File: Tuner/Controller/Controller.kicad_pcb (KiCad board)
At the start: 2 copper layers, 96.8 x 99.3 mm, 175 parts, among them J1 Conn_02x05_Odd_Even, J10 Conn_01x05, J11 Conn_01x01, J12 Conn_01x02, J14 Conn_01x01, J15 Conn_01x02, J16 Conn_01x06, J17 Conn_01x01, J18 Conn_01x01, J19 Conn_01x01, J2 Conn_02x05_Odd_Even, J20 Conn_01x01, J21 Conn_01x01, J23 Conn_01x01, J26 Conn_01x02, J27 Conn_01x02, J28 Conn_01x02, J3 Conn_02x05_Odd_Even, J30 Conn_01x02, J4 Conn_02x05_Odd_Even, J5 Conn_02x05_Odd_Even, J6 Conn_01x02, J7 Conn_01x02, J8 Conn_01x06, Q1 2N3904, Q2 2N3904, Q3 2N3904, Q4 2N3904, Q5 2N3904, Q6 2N3904, Q7 2N3904, Q8 2N3904, U1 74LS393, U2 74HC14, U3 74HC86, U4 LM350_TO220

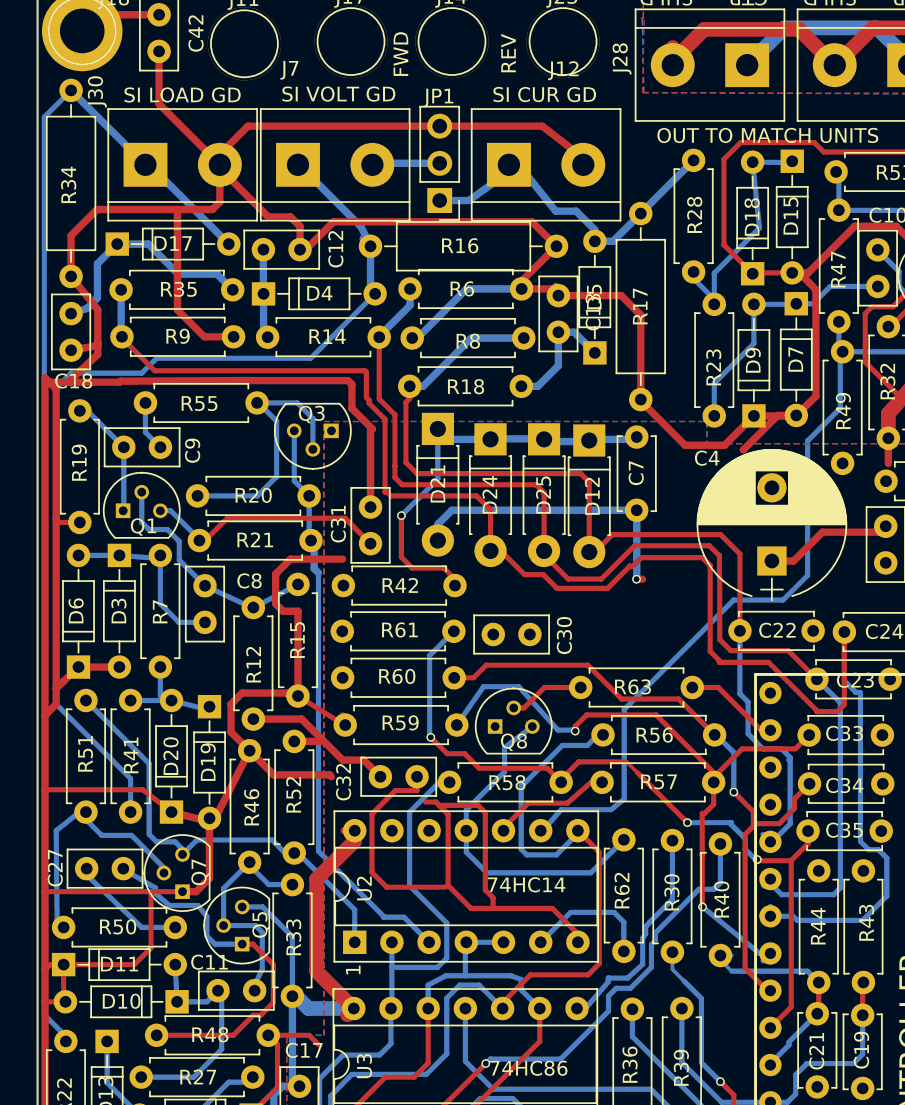
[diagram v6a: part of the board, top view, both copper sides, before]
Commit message: Fixed TandemMatch grounding problem
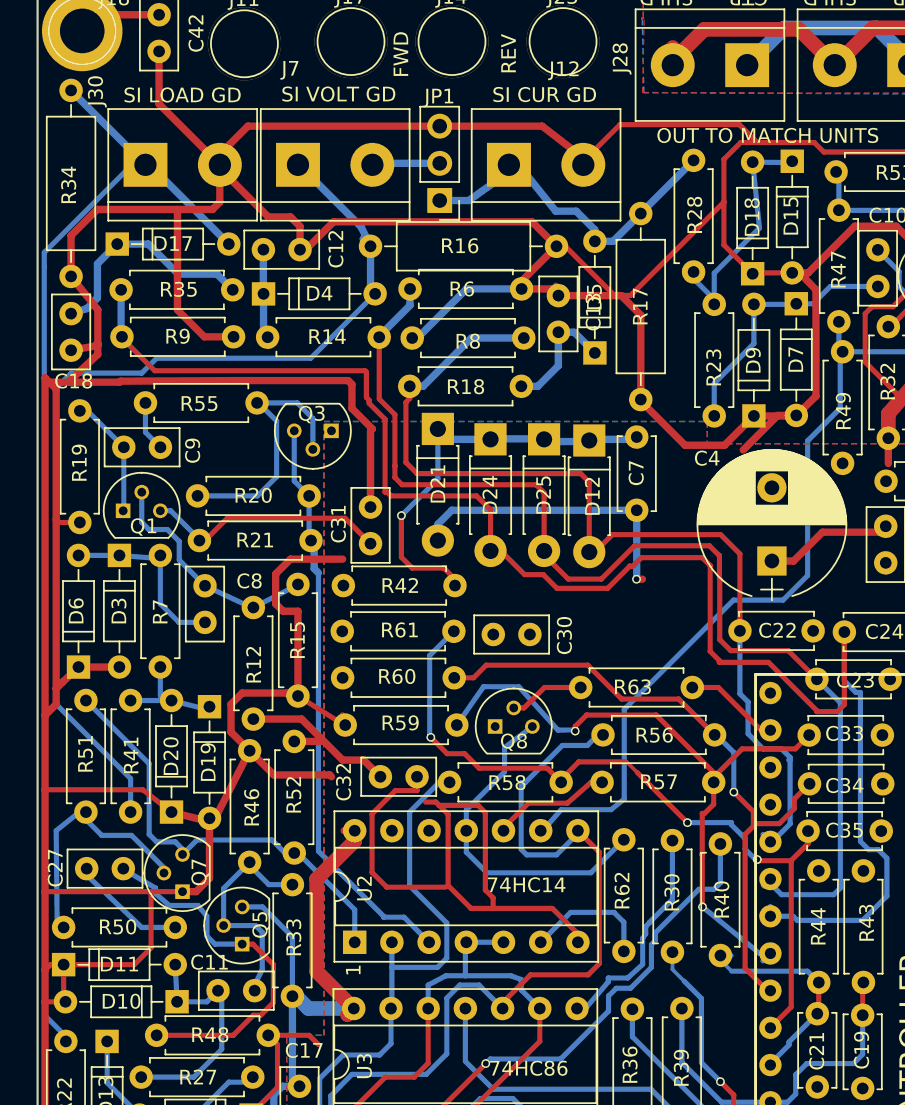
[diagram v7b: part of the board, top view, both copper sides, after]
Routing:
- net GND: track 622.5 -> 652.1 mm
- net XCur: track 82.0 -> 79.5 mm
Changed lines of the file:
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@@
     (thickness 1.6)
     (drawings 57)
-    (tracks 1583)
+    (tracks 1597)
     (zones 0)
     (modules 175)
@@
   )
   (setup
-    (last_trace_width 0.5)
+    (last_trace_width 0.35)
     (user_trace_width 0.35)
     (user_trace_width 0.5)
@@
   (segment (start 76.5302 99.187) (end 76.962 98.7552) (width 0.5) (layer F.Cu) (net 5) (status 30))
   (segment (start 77.0255 86.614) (end 76.30414 86.614) (width 0.5) (layer F.Cu) (net 5) (status 30))
+  (segment (start 94.7547 50.0634) (end 95.8596 50.0634) (width 0.35) (layer F.Cu) (net 6))
+  (segment (start 95.8596 50.0634) (end 102.235 43.688) (width 0.35) (layer F.Cu) (net 6))
+  (segment (start 90.805 46.7106) (end 91.4019 46.7106) (width 0.35) (layer F.Cu) (net 6))
+  (segment (start 91.4019 46.7106) (end 94.7547 50.0634) (width 0.35) (layer F.Cu) (net 6))
+  (segment (start 94.7547 50.0634) (end 94.7693 50.078) (width 0.35) (layer F.Cu) (net 6))
+  (segment (start 94.7693 50.078) (end 95.22904 50.078) (width 0.35) (layer F.Cu) (net 6))
+  (segment (start 92.6338 41.148) (end 92.6338 40.9067) (width 0.35) (layer F.Cu) (net 6))
+  (segment (start 92.6338 40.9067) (end 95.1357 38.4048) (width 0.35) (layer F.Cu) (net 6))
+  (segment (start 103.2891 38.4048) (end 104.5083 39.624) (width 0.35) (layer F.Cu) (net 6))
+  (segment (start 95.1357 38.4048) (end 103.2891 38.4048) (width 0.35) (layer F.Cu) (net 6))
   (segment (start 82.8294 38.5064) (end 89.8271 38.5064) (width 0.5) (layer F.Cu) (net 6) (status 10))
   (segment (start 89.8271 38.5064) (end 92.6338 40.67302) (width 0.5) (layer F.Cu) (net 6) (status 20))
@@
   (segment (start 109.0549 40.2717) (end 118.0338 40.2717) (width 0.35) (layer F.Cu) (net 6))
   (segment (start 108.4072 39.624) (end 109.0549 40.2717) (width 0.35) (layer F.Cu) (net 6))
-  (segment (start 102.235 40.767) (end 102.235 46.62424) (width 0.35) (layer F.Cu) (net 6))
-  (segment (start 104.19588 48.58512) (end 102.235 46.62424) (width 0.35) (layer F.Cu) (net 6) (status 10))
+  (segment (start 102.235 40.767) (end 102.235 43.688) (width 0.35) (layer F.Cu) (net 6))
+  (segment (start 103.378 39.624) (end 104.5083 39.624) (width 0.35) (layer F.Cu) (net 6))
   (segment (start 102.235 40.767) (end 103.378 39.624) (width 0.35) (layer F.Cu) (net 6))
+  (segment (start 102.235 43.688) (end 102.235 46.62424) (width 0.35) (layer F.Cu) (net 6))
+  (segment (start 104.19588 48.58512) (end 102.235 46.62424) (width 0.35) (layer F.Cu) (net 6) (status 10))
   (segment (start 123.317 42.6085) (end 124.206 43.053) (width 0.35) (layer F.Cu) (net 6))
-  (segment (start 103.378 39.624) (end 108.4072 39.624) (width 0.35) (layer F.Cu) (net 6))
+  (segment (start 104.5083 39.624) (end 108.4072 39.624) (width 0.35) (layer F.Cu) (net 6))
   (segment (start 140.3604 56.0578) (end 142.2654 56.0578) (width 0.35) (layer F.Cu) (net 6) (status 10))
   (via (at 142.3162 54.0766) (size 0.6) (drill 0.4) (layers F.Cu B.Cu) (net 6))
@@
   (segment (start 58.25744 57.94756) (end 58.77242 57.94756) (width 0.35) (layer B.Cu) (net 36) (status 30))
   (segment (start 58.77242 57.94756) (end 61.25908 60.43422) (width 0.35) (layer B.Cu) (net 36) (status 30))
+  (segment (start 55.8292 48.11268) (end 55.8292 47.1297) (width 0.35) (layer B.Cu) (net 37))
+  (segment (start 55.8292 47.1297) (end 61.8109 41.148) (width 0.35) (layer B.Cu) (net 37) (status 800000))
+  (segment (start 61.8109 41.148) (end 62.738 41.148) (width 0.35) (layer B.Cu) (net 37) (status C00000))
   (segment (start 57.3024 101.0031) (end 57.3024 100.6602) (width 0.35) (layer B.Cu) (net 37) (status 30))
   (segment (start 57.3024 100.6602) (end 55.8292 99.187) (width 0.35) (layer B.Cu) (net 37) (status 10))
-  (segment (start 55.8292 99.187) (end 55.8292 37.8968) (width 0.35) (layer B.Cu) (net 37))
-  (segment (start 55.8292 37.8968) (end 57.658 36.068) (width 0.35) (layer B.Cu) (net 37) (status 20))
+  (segment (start 55.8292 99.187) (end 55.8292 48.11268) (width 0.35) (layer B.Cu) (net 37))
   (segment (start 57.658 36.068) (end 57.658 36.6014) (width 0.5) (layer F.Cu) (net 37) (status 30))
   (segment (start 62.738 41.148) (end 63.0174 41.148) (width 0.5) (layer B.Cu) (net 37) (status 30))
@@
   (segment (start 133.6929 34.3662) (end 133.6929 35.5219) (width 1) (layer F.Cu) (net 93))
   (segment (start 133.6929 35.5219) (end 135.382 37.211) (width 1) (layer F.Cu) (net 93))
-  (segment (start 146.9898 42.1386) (end 149.9616 43.815) (width 1) (layer F.Cu) (net 93) (status 800000))
+  (segment (start 146.9898 42.1386) (end 149.9616 43.815) (width 1) (layer F.Cu) (net 93))
   (segment (start 146.9898 39.1922) (end 146.9898 42.1386) (width 1) (layer F.Cu) (net 93))
   (segment (start 145.1229 37.1856) (end 146.9898 39.1922) (width 1) (layer F.Cu) (net 93))

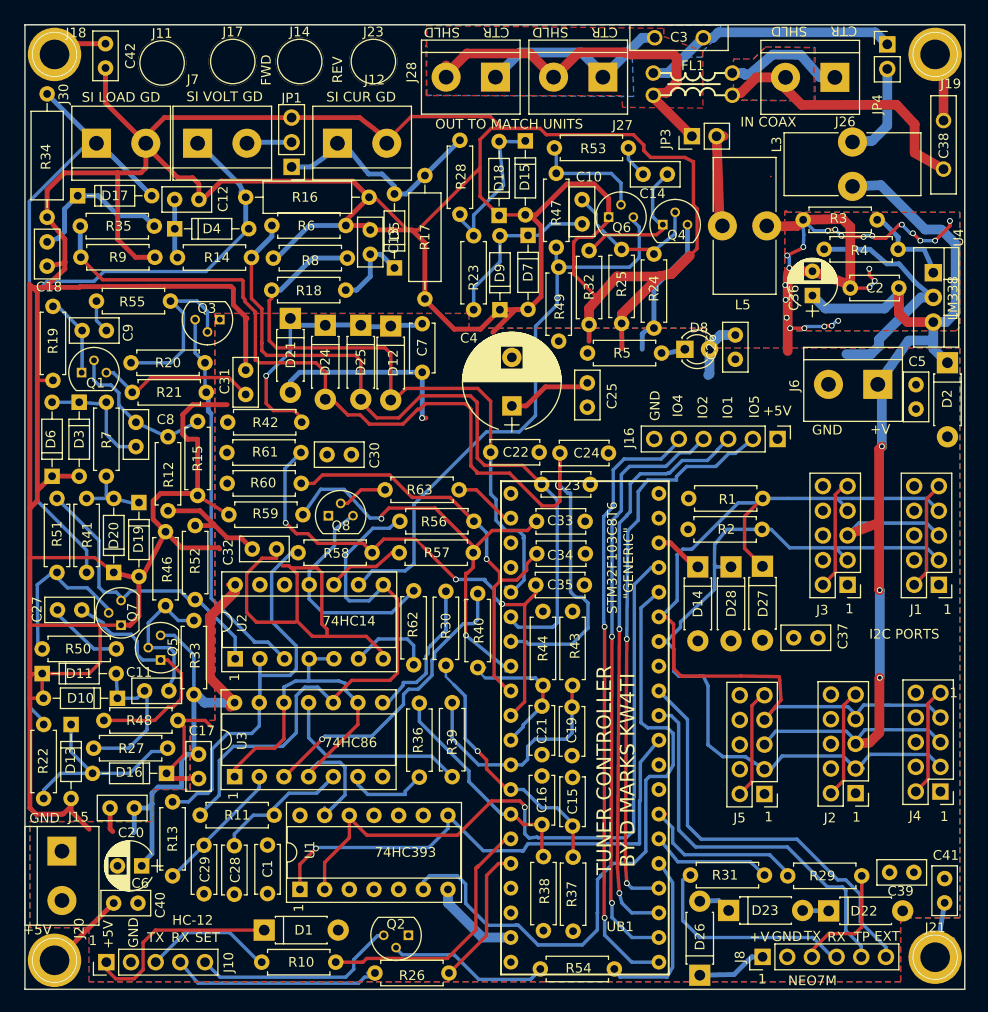
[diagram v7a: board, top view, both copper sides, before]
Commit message: Removed 1k resistors, did some more rearranging on TandemMatch
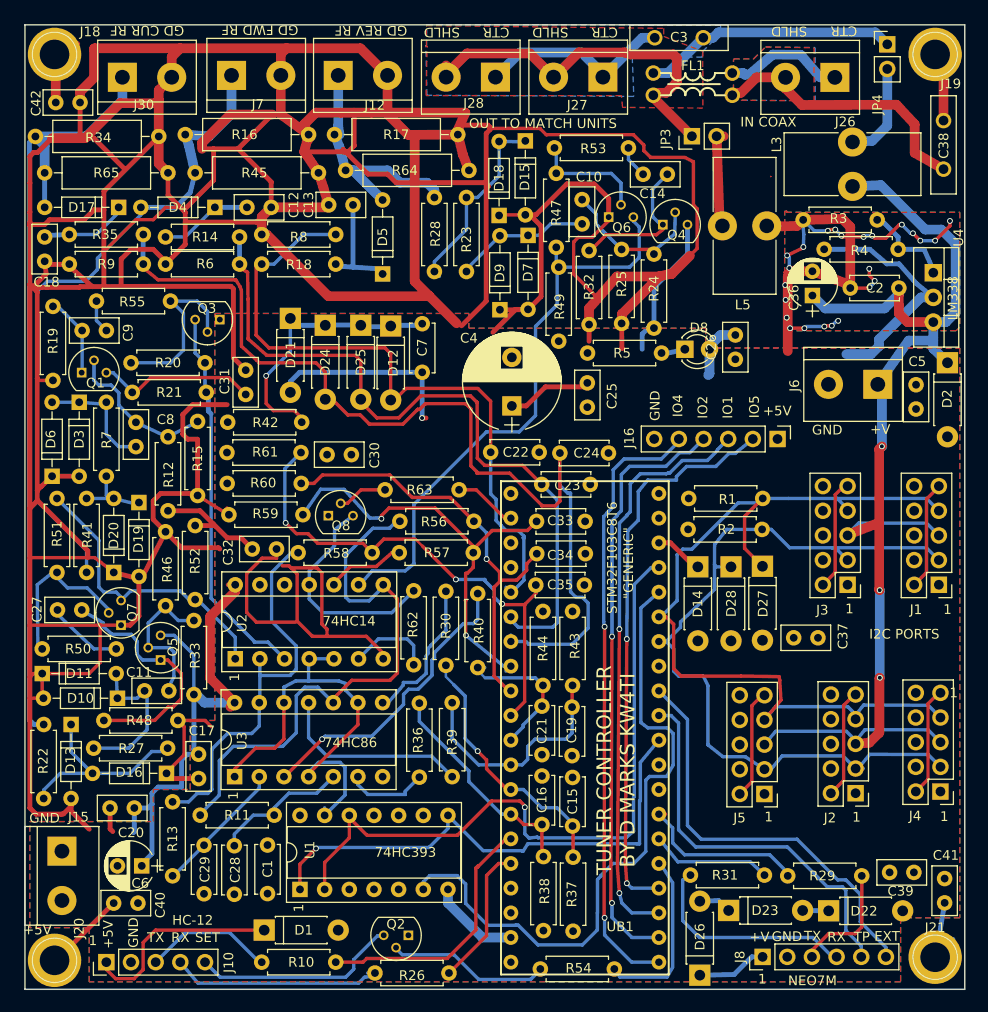
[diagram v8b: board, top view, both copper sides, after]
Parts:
- removed J11, J14, J17, J23: Conn_01x01, Connectors:1pin
- removed JP1: Jumper_NC_Dual, Pin_Headers:Pin_Header_Straight_1x03_Pitch2.54mm
- added R45: 33R, Resistors_THT:R_Axial_DIN0309_L9.0mm_D3.2mm_P12.70mm_Horizontal, F.Cu at (72.9, 44.2)
- added R64: 33R, Resistors_THT:R_Axial_DIN0309_L9.0mm_D3.2mm_P12.70mm_Horizontal, F.Cu at (88.4, 43.9)
- added R65: 33R, Resistors_THT:R_Axial_DIN0309_L9.0mm_D3.2mm_P12.70mm_Horizontal, F.Cu at (57.4, 44.2)
- R16, R17, R34: value 50R -> 33R
- moved R17 10.2 mm to (87.2, 40.3), turned to 0 degrees
- moved R16 8.96 mm to (71.9, 40.3)
- moved R35 8.79 mm to (59.9, 50.5), turned to 0 degrees
- moved C42 7.93 mm to (58.5, 37.0), turned to 0 degrees
- moved J7 7.81 mm to (76.6, 34.2)
- moved C12 7.49 mm to (78.2, 47.8)
- moved J30 7.30 mm to (65.4, 34.4)
- moved J12 6.99 mm to (87.6, 34.2)
- moved R9 6.47 mm to (67.6, 53.6), turned to 180 degrees
- moved R28 6.45 mm to (97.5, 46.7)
- moved C13 5.38 mm to (89.2, 47.5), turned to 180 degrees
- moved R6 5.19 mm to (77.5, 53.6), turned to 180 degrees
- moved D4 4.68 mm to (74.9, 47.8), turned to 180 degrees
- moved R34 4.54 mm to (56.5, 40.4), turned to 0 degrees
- moved D17 4.38 mm to (65.0, 47.8), turned to 180 degrees
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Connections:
- J7 pad 2: Net-(J7-Pad2) -> GND
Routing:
- net GND: track 652.1 -> 833.7 mm
- net VCur: track 111.0 -> 102.8 mm
- net Net-(C18-Pad1): track 15.6 -> 9.90 mm
- net Net-(J7-Pad2): track 4.91 -> 0.00 mm
- net Net-(C12-Pad1): track 6.10 -> 10.7 mm
- net VRev: track 68.2 -> 72.0 mm
- net Net-(C10-Pad1): track 18.4 -> 14.7 mm
- net XCur: track 79.5 -> 82.9 mm
- net Net-(D15-Pad1): track 17.6 -> 19.8 mm
- net Net-(C13-Pad1): track 9.43 -> 11.6 mm
- net VFwd: track 79.4 -> 77.9 mm
- net XRev: track 24.3 -> 25.7 mm
- net Net-(C42-Pad1): track 5.70 -> 6.56 mm
- net XFwd: track 68.9 -> 68.1 mm
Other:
- board text added: "GD CUR RF"
- board text added: "GD FWD RF"
- board text added: "GD REV RF"
- board text removed: "FWD"
- board text removed: "REV"
- board text removed: "SI CUR GD"
- board text removed: "SI LOAD GD"
- board text removed: "SI VOLT GD"
